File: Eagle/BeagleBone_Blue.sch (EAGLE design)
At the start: 175 parts, among them M1 JST_ZH_2, M2 JST_ZH_2, M3 JST_ZH_2, M4 JST_ZH_2, Q3 MOSFET-N, U1 OSD3358, U2 CM200C-32.768KAZF-UT, U5 24LC_32AT-I/OT, U6 SN74LVC1G07_DCK_5, Y2 445C33D24M00000

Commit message: Stopping for the night
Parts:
- added U3: SCHA5B0200, SCHA5B0200:SCHA5B0200
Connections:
- net PWM_1A: now also U1B.EHRPWM1A_U14
- net PWM_1B: now also U1B.EHRPWM1B_T14
- net PWM_2A: now also U1B.EHRPWM2A_U10
- net PWM_2B: now also U1B.EHRPWM2B_T10
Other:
- moved on the sheet: D10, D11, D12, D13, R61, R62, R63, R64
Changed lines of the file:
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@@
 <part name="R63" library="Strawson_Eagle_Lib" deviceset="RESISTOR" device="0402-RES" value="261"/>
 <part name="R64" library="Strawson_Eagle_Lib" deviceset="RESISTOR" device="0402-RES" value="261"/>
+<part name="U3" library="SCHA5B0200" deviceset="SCHA5B0200" device=""/>
 </parts>
 <sheets>
@@
 <instance part="C33" gate="G$1" x="345.44" y="231.14"/>
 <instance part="R60" gate="G$1" x="345.44" y="246.38" rot="R90"/>
-<instance part="D10" gate="G$1" x="246.38" y="142.24" rot="R270"/>
-<instance part="D11" gate="G$1" x="254" y="139.7" rot="R270"/>
-<instance part="D12" gate="G$1" x="261.62" y="137.16" rot="R270"/>
-<instance part="D13" gate="G$1" x="269.24" y="134.62" rot="R270"/>
-<instance part="R61" gate="G$1" x="208.28" y="142.24"/>
-<instance part="R62" gate="G$1" x="218.44" y="139.7"/>
-<instance part="R63" gate="G$1" x="228.6" y="137.16"/>
-<instance part="R64" gate="G$1" x="238.76" y="134.62"/>
+<instance part="D10" gate="G$1" x="223.52" y="142.24" rot="R270"/>
+<instance part="D11" gate="G$1" x="231.14" y="139.7" rot="R270"/>
+<instance part="D12" gate="G$1" x="238.76" y="137.16" rot="R270"/>
+<instance part="D13" gate="G$1" x="246.38" y="134.62" rot="R270"/>
+<instance part="R61" gate="G$1" x="193.04" y="142.24"/>
+<instance part="R62" gate="G$1" x="200.66" y="139.7"/>
+<instance part="R63" gate="G$1" x="208.28" y="137.16"/>
+<instance part="R64" gate="G$1" x="215.9" y="134.62"/>
+<instance part="U3" gate="G$1" x="195.58" y="99.06"/>
 </instances>
 <busses>
@@
 <segment>
 <pinref part="R59" gate="G$1" pin="1"/>
-<wire x1="248.92" y1="149.86" x2="195.58" y2="149.86" width="0.1524" layer="91"/>
+<wire x1="248.92" y1="149.86" x2="187.96" y2="149.86" width="0.1524" layer="91"/>
 <label x="182.88" y="149.86" size="1.778" layer="95"/>
 <pinref part="R64" gate="G$1" pin="1"/>
-<wire x1="195.58" y1="149.86" x2="182.88" y2="149.86" width="0.1524" layer="91"/>
-<wire x1="233.68" y1="134.62" x2="195.58" y2="134.62" width="0.1524" layer="91"/>
-<wire x1="195.58" y1="134.62" x2="195.58" y2="137.16" width="0.1524" layer="91"/>
-<junction x="195.58" y="149.86"/>
+<wire x1="187.96" y1="149.86" x2="182.88" y2="149.86" width="0.1524" layer="91"/>
+<wire x1="210.82" y1="134.62" x2="187.96" y2="134.62" width="0.1524" layer="91"/>
+<wire x1="187.96" y1="134.62" x2="187.96" y2="137.16" width="0.1524" layer="91"/>
+<junction x="187.96" y="149.86"/>
 <pinref part="R63" gate="G$1" pin="1"/>
-<wire x1="195.58" y1="137.16" x2="195.58" y2="139.7" width="0.1524" layer="91"/>
-<wire x1="195.58" y1="139.7" x2="195.58" y2="142.24" width="0.1524" layer="91"/>
-<wire x1="195.58" y1="142.24" x2="195.58" y2="149.86" width="0.1524" layer="91"/>
-<wire x1="223.52" y1="137.16" x2="195.58" y2="137.16" width="0.1524" layer="91"/>
-<junction x="195.58" y="137.16"/>
+<wire x1="187.96" y1="137.16" x2="187.96" y2="139.7" width="0.1524" layer="91"/>
+<wire x1="187.96" y1="139.7" x2="187.96" y2="142.24" width="0.1524" layer="91"/>
+<wire x1="187.96" y1="142.24" x2="187.96" y2="149.86" width="0.1524" layer="91"/>
+<wire x1="203.2" y1="137.16" x2="187.96" y2="137.16" width="0.1524" layer="91"/>
+<junction x="187.96" y="137.16"/>
 <pinref part="R62" gate="G$1" pin="1"/>
-<wire x1="213.36" y1="139.7" x2="195.58" y2="139.7" width="0.1524" layer="91"/>
-<junction x="195.58" y="139.7"/>
+<wire x1="195.58" y1="139.7" x2="187.96" y2="139.7" width="0.1524" layer="91"/>
+<junction x="187.96" y="139.7"/>
 <pinref part="R61" gate="G$1" pin="1"/>
-<wire x1="203.2" y1="142.24" x2="195.58" y2="142.24" width="0.1524" layer="91"/>
-<junction x="195.58" y="142.24"/>
+<junction x="187.96" y="142.24"/>
 </segment>
 <segment>
@@
 <pinref part="U1" gate="B" pin="USR3_V16"/>
 <pinref part="D13" gate="G$1" pin="A"/>
-<wire x1="281.94" y1="134.62" x2="271.78" y2="134.62" width="0.1524" layer="91"/>
+<wire x1="281.94" y1="134.62" x2="248.92" y2="134.62" width="0.1524" layer="91"/>
 </segment>
 </net>
@@
 <pinref part="U1" gate="B" pin="USR2_T15"/>
 <pinref part="D12" gate="G$1" pin="A"/>
-<wire x1="281.94" y1="137.16" x2="264.16" y2="137.16" width="0.1524" layer="91"/>
+<wire x1="281.94" y1="137.16" x2="241.3" y2="137.16" width="0.1524" layer="91"/>
 </segment>
 </net>
@@
 <pinref part="U1" gate="B" pin="USR1_U15"/>
 <pinref part="D11" gate="G$1" pin="A"/>
-<wire x1="281.94" y1="139.7" x2="256.54" y2="139.7" width="0.1524" layer="91"/>
+<wire x1="281.94" y1="139.7" x2="233.68" y2="139.7" width="0.1524" layer="91"/>
 </segment>
 </net>
@@
 <pinref part="U1" gate="B" pin="USR0_V15"/>
 <pinref part="D10" gate="G$1" pin="A"/>
-<wire x1="281.94" y1="142.24" x2="248.92" y2="142.24" width="0.1524" layer="91"/>
+<wire x1="281.94" y1="142.24" x2="226.06" y2="142.24" width="0.1524" layer="91"/>
 </segment>
 </net>
@@
 <pinref part="D10" gate="G$1" pin="C"/>
 <pinref part="R61" gate="G$1" pin="2"/>
-<wire x1="241.3" y1="142.24" x2="213.36" y2="142.24" width="0.1524" layer="91"/>
+<wire x1="218.44" y1="142.24" x2="198.12" y2="142.24" width="0.1524" layer="91"/>
 </segment>
 </net>
@@
 <pinref part="D11" gate="G$1" pin="C"/>
 <pinref part="R62" gate="G$1" pin="2"/>
-<wire x1="248.92" y1="139.7" x2="223.52" y2="139.7" width="0.1524" layer="91"/>
+<wire x1="226.06" y1="139.7" x2="205.74" y2="139.7" width="0.1524" layer="91"/>
 </segment>
 </net>
@@
 <pinref part="D12" gate="G$1" pin="C"/>
 <pinref part="R63" gate="G$1" pin="2"/>
-<wire x1="256.54" y1="137.16" x2="233.68" y2="137.16" width="0.1524" layer="91"/>
+<wire x1="233.68" y1="137.16" x2="213.36" y2="137.16" width="0.1524" layer="91"/>
 </segment>
 </net>
@@
 <pinref part="D13" gate="G$1" pin="C"/>
 <pinref part="R64" gate="G$1" pin="2"/>
-<wire x1="264.16" y1="134.62" x2="243.84" y2="134.62" width="0.1524" layer="91"/>
+<wire x1="241.3" y1="134.62" x2="220.98" y2="134.62" width="0.1524" layer="91"/>
+</segment>
+</net>
+<net name="PWM_2B" class="0">
+<segment>
+<pinref part="U1" gate="B" pin="EHRPWM2B_T10"/>
+<wire x1="281.94" y1="129.54" x2="256.54" y2="129.54" width="0.1524" layer="91"/>
+<label x="256.54" y="129.54" size="1.778" layer="95"/>
+</segment>
+</net>
+<net name="PWM_2A" class="0">
+<segment>
+<pinref part="U1" gate="B" pin="EHRPWM2A_U10"/>
+<wire x1="281.94" y1="127" x2="256.54" y2="127" width="0.1524" layer="91"/>
+<label x="256.54" y="127" size="1.778" layer="95"/>
+</segment>
+</net>
+<net name="PWM_1B" class="0">
+<segment>
+<pinref part="U1" gate="B" pin="EHRPWM1B_T14"/>
+<wire x1="281.94" y1="124.46" x2="256.54" y2="124.46" width="0.1524" layer="91"/>
+<label x="256.54" y="124.46" size="1.778" layer="95"/>
+</segment>
+</net>
+<net name="PWM_1A" class="0">
+<segment>
+<pinref part="U1" gate="B" pin="EHRPWM1A_U14"/>
+<wire x1="281.94" y1="121.92" x2="256.54" y2="121.92" width="0.1524" layer="91"/>
+<label x="256.54" y="121.92" size="1.778" layer="95"/>
 </segment>
 </net>

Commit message: working on ERCs
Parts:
- renumbered U1 to SIP

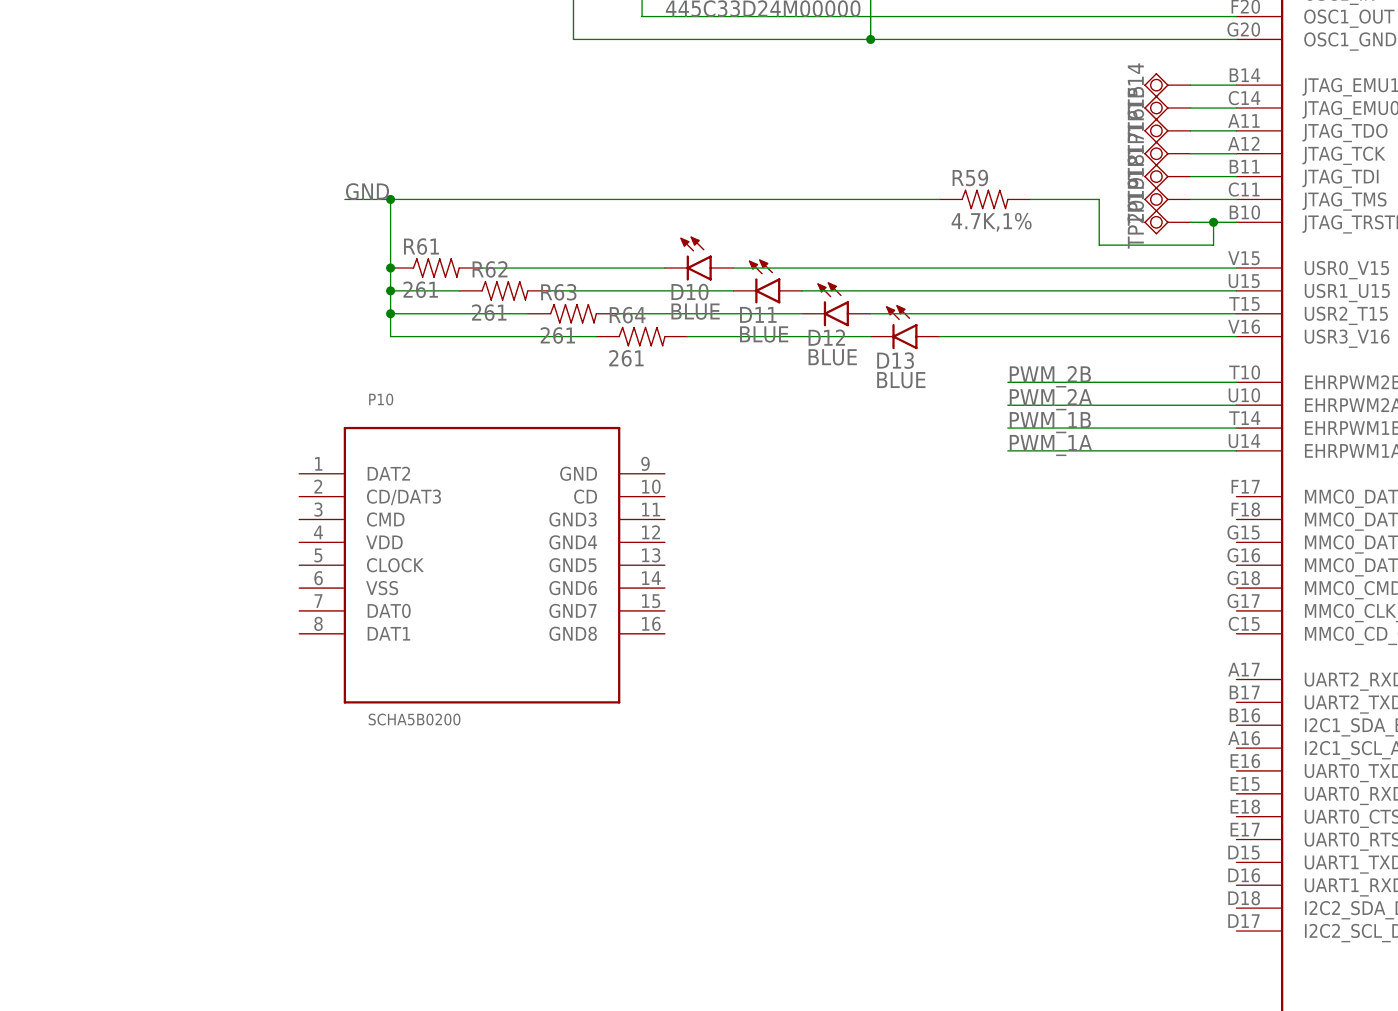
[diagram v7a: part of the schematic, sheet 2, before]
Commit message: Add uSD card
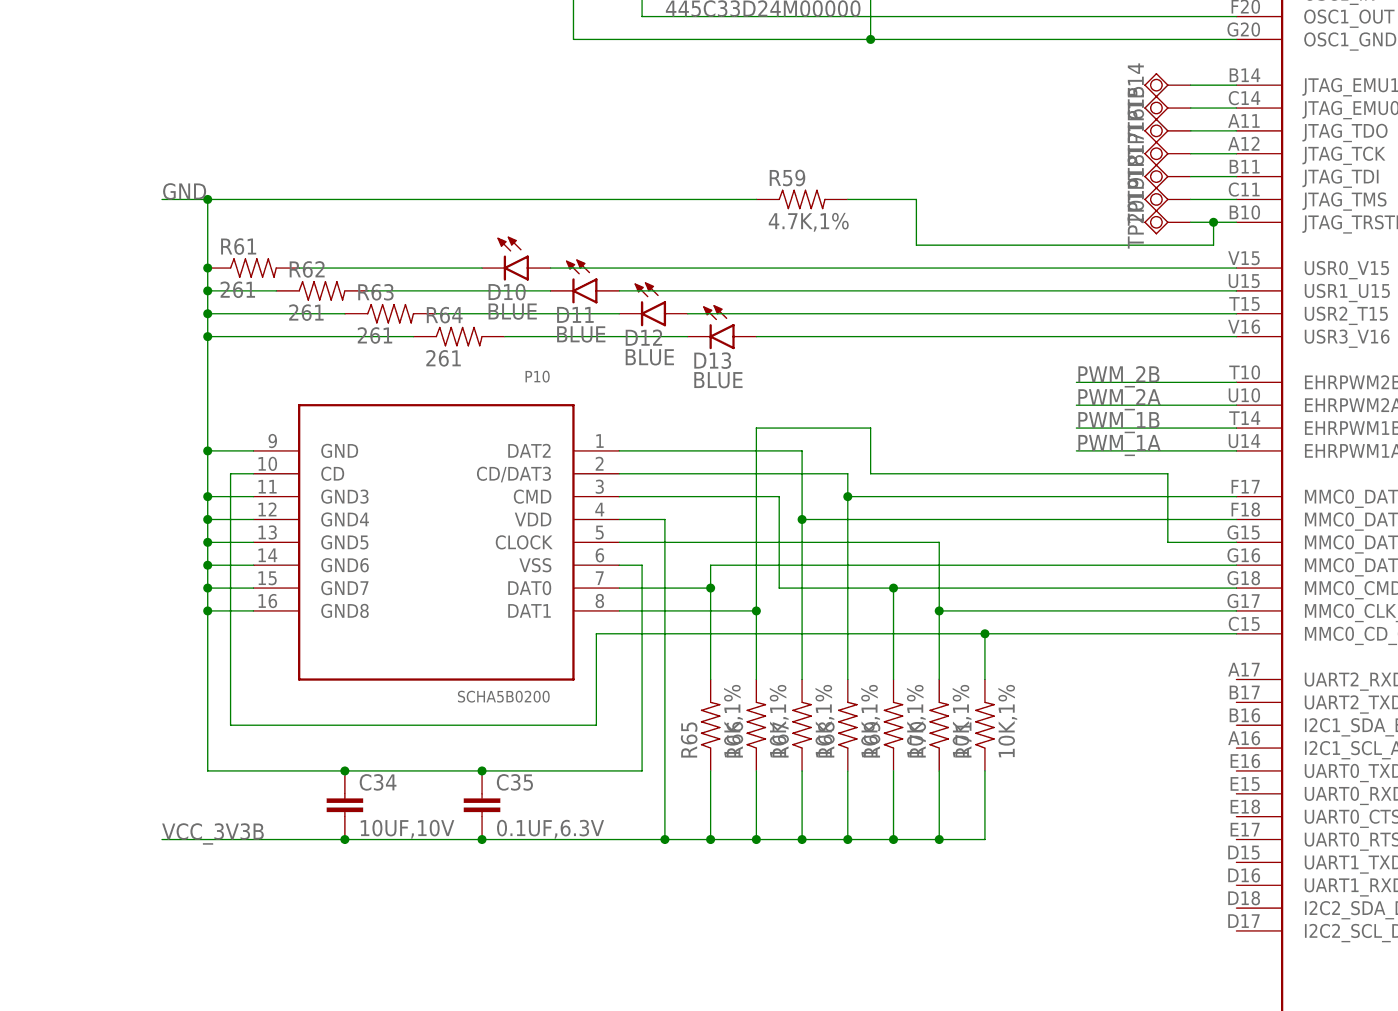
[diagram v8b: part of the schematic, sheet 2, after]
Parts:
- added C34: 10UF,10V, Strawson_Eagle_Lib:CAP0805
- added C35: 0.1UF,6.3V, Strawson_Eagle_Lib:CAP0402-CAP
- added R65, R66, R67, R68, R69, R70, R71: 10K,1%, Strawson_Eagle_Lib:RESISTOR0402-RES
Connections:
- new net N$64: R68.2, SIPB.MMC0_DAT3_F17, U3.CD/DAT3
- new net N$70: R66.2, SIPB.MMC0_DAT1_G15, U3.DAT1
- new net N$73: R70.2, SIPB.MMC0_CLK_G17, U3.CLOCK
- new net N$74: R69.2, SIPB.MMC0_CMD_G18, U3.CMD
- new net N$75: R71.2, SIPB.MMC0_CD_C15, U3.CD
- new net N$77: R65.2, SIPB.MMC0_DAT0_G16, U3.DAT0
- new net NTE: R67.2, SIPB.MMC0_DAT2_F18, U3.DAT2
- new net VCC_3V3B: C34.2, C35.2, R65.1, R66.1, R67.1, R68.1, R69.1, R70.1, R71.1, U3.VDD
- net GND: now also C34.1, C35.1, U3.GND, U3.GND3, U3.GND4, U3.GND5, U3.GND6, U3.GND7, U3.GND8, U3.VSS
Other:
- moved on the sheet: D10, D11, D12, D13, R59, R61, R62, R63, R64
